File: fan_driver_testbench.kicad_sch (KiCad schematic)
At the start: 6 parts, among them Q5 BTS141

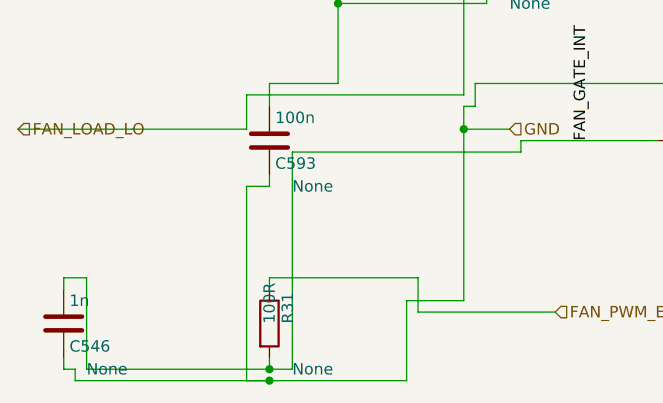
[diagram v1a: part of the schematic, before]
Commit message: optimazed load to kicad
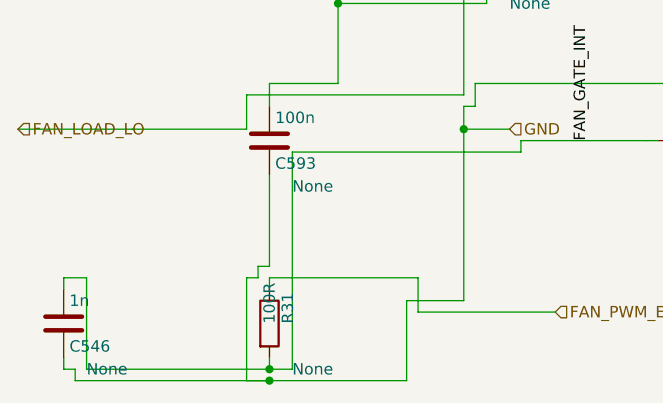
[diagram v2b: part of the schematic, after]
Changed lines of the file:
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@@
 		(instances
 			(project "Untitled"
-				(path "/4b1f6fb3-968a-4690-9ff6-6727556273b3"
+				(path "/bf864d83-638d-4400-a181-9f7b7e09d144"
 					(reference "R31")
 					(unit 1)
@@
 		(instances
 			(project "Untitled"
-				(path "/4b1f6fb3-968a-4690-9ff6-6727556273b3"
+				(path "/bf864d83-638d-4400-a181-9f7b7e09d144"
 					(reference "C546")
 					(unit 1)
@@
 		(instances
 			(project "Untitled"
-				(path "/4b1f6fb3-968a-4690-9ff6-6727556273b3"
+				(path "/bf864d83-638d-4400-a181-9f7b7e09d144"
 					(reference "Q5")
 					(unit 1)
@@
 		(instances
 			(project "Untitled"
-				(path "/4b1f6fb3-968a-4690-9ff6-6727556273b3"
+				(path "/bf864d83-638d-4400-a181-9f7b7e09d144"
 					(reference "D6")
 					(unit 1)
@@
 		(instances
 			(project "Untitled"
-				(path "/4b1f6fb3-968a-4690-9ff6-6727556273b3"
+				(path "/bf864d83-638d-4400-a181-9f7b7e09d144"
 					(reference "L637")
 					(unit 1)
@@
 		(instances
 			(project "Untitled"
-				(path "/4b1f6fb3-968a-4690-9ff6-6727556273b3"
+				(path "/bf864d83-638d-4400-a181-9f7b7e09d144"
 					(reference "C593")
 					(unit 1)
@@
 	(wire
 		(pts
-			(xy 31.75 33.02) (xy 29.21 33.02)
-		)
-		(stroke
-			(width 0)
-			(type default)
-		)
-	)
-	(wire
-		(pts
-			(xy 29.21 33.02) (xy 29.21 54.61)
-		)
-		(stroke
+			(xy 31.75 33.02) (xy 31.75 41.91)
+		)
+		(stroke
+			(width 0)
+			(type default)
+		)
+	)
+	(wire
+		(pts
+			(xy 31.75 41.91) (xy 30.48 41.91)
+		)
+		(stroke
+			(width 0)
+			(type default)
+		)
+	)
+	(wire
+		(pts
+			(xy 30.48 41.91) (xy 30.48 43.18)
+		)
+		(stroke
+			(width 0)
+			(type default)
+		)
+	)
+	(wire
+		(pts
+			(xy 30.48 43.18) (xy 29.21 43.18)
+		)
+		(stroke
+			(width 0)
+			(type default)
+		)
+	)
+	(wire
+		(pts
+			(xy 29.21 43.18) (xy 29.21 54.61)
+		)
+		(stroke

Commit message: tests_fix
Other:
- title: (none) -> climate_control_niva_travel
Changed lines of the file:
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@@
 	(generator_version "9.0")
 	(paper "A4")
+	(title_block
+		(title "climate_control_niva_travel")
+	)
 	(symbol
 		(lib_id "Device:R")
@@
 		)
 		(instances
-			(project "Untitled"
-				(path "/bf864d83-638d-4400-a181-9f7b7e09d144"
+			(project "climate_control_niva_travel"
+				(path "/769b9906-d389-4980-b175-619cd77c101f"
 					(reference "R31")
 					(unit 1)
@@
 		)
 		(instances
-			(project "Untitled"
-				(path "/bf864d83-638d-4400-a181-9f7b7e09d144"
+			(project "climate_control_niva_travel"
+				(path "/769b9906-d389-4980-b175-619cd77c101f"
 					(reference "C546")
 					(unit 1)
@@
 		)
 		(instances
-			(project "Untitled"
-				(path "/bf864d83-638d-4400-a181-9f7b7e09d144"
+			(project "climate_control_niva_travel"
+				(path "/769b9906-d389-4980-b175-619cd77c101f"
 					(reference "Q5")
 					(unit 1)
@@
 		)
 		(instances
-			(project "Untitled"
-				(path "/bf864d83-638d-4400-a181-9f7b7e09d144"
+			(project "climate_control_niva_travel"
+				(path "/769b9906-d389-4980-b175-619cd77c101f"
 					(reference "D6")
 					(unit 1)
@@
 		)
 		(instances
-			(project "Untitled"
-				(path "/bf864d83-638d-4400-a181-9f7b7e09d144"
+			(project "climate_control_niva_travel"
+				(path "/769b9906-d389-4980-b175-619cd77c101f"
 					(reference "L637")
 					(unit 1)
@@
 		)
 		(instances
-			(project "Untitled"
-				(path "/bf864d83-638d-4400-a181-9f7b7e09d144"
+			(project "climate_control_niva_travel"
+				(path "/769b9906-d389-4980-b175-619cd77c101f"
 					(reference "C593")
 					(unit 1)
@@
 	(junction
 		(at 31.75 54.61)
+		(diameter 0)
+		(color 0 0 0 0)
+	)
+	(junction
+		(at 67.31 27.94)
 		(diameter 0)
 		(color 0 0 0 0)
@@
 		)
 	)
+	(hierarchical_label "FAN_LOAD_LO"
+		(shape output)
+		(at 3.81 26.67 0)
+		(effects
+			(font
+				(size 1.27 1.27)
+			)
+			(justify left)
+		)
+	)
+	(hierarchical_label "MOTOR_TERM"
+		(shape output)
+		(at 26.67 6.35 0)
+		(effects
+			(font
+				(size 1.27 1.27)
+			)
+			(justify left)
+		)
+	)
 	(hierarchical_label "VBAT_FAN"
 		(shape input)
@@
 		(effects
 			(font
-				(size 1.27 1.27)
-			)
-			(justify left)
-		)
-	)
-	(hierarchical_label "FAN_LOAD_LO"
-		(shape input)
-		(at 3.81 26.67 0)
-		(effects
-			(font
-				(size 1.27 1.27)
-			)
-			(justify left)
-		)
-	)
-	(hierarchical_label "MOTOR_TERM"
-		(shape input)
-		(at 26.67 6.35 0)
-		(effects
-			(font

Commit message: refactoring
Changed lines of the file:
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@@
+			)
+		)
+		(property "Sim.Device" "R"
+			(at 34.29 53.3399 0)
+			(effects
+				(font
+					(size 1.27 1.27)
+				)
+				(justify left)
+			)
+		)
+		(property "Sim.Params" "R=100R"
+			(at 34.29 53.3399 0)
+			(effects
+				(font
+					(size 1.27 1.27)
+				)
+				(justify left)
 			)
 		)
@@
 		(instances
 			(project "climate_control_niva_travel"
-				(path "/769b9906-d389-4980-b175-619cd77c101f"
+				(path "/04e9baa8-05c1-4d46-8e7f-66f0ccb7f2e0"
 					(reference "R31")
 					(unit 1)
@@
 			)
 		)
+		(property "Sim.Device" "C"
+			(at 11.43 53.3399 0)
+			(effects
+				(font
+					(size 1.27 1.27)
+				)
+				(justify left)
+			)
+		)
+		(property "Sim.Params" "C=1n"
+			(at 11.43 53.3399 0)
+			(effects
+				(font
+					(size 1.27 1.27)
+				)
+				(justify left)
+			)
+		)
 		(pin "1"
 		)
@@
 		(instances
 			(project "climate_control_niva_travel"
-				(path "/769b9906-d389-4980-b175-619cd77c101f"
+				(path "/04e9baa8-05c1-4d46-8e7f-66f0ccb7f2e0"
 					(reference "C546")
 					(unit 1)
@@
 			)
 		)
+		(property "Sim.Device" "X"
+			(at 82.55 33.0199 0)
+			(effects
+				(font
+					(size 1.27 1.27)
+				)
+				(justify left)
+			)
+		)
+		(property "Sim.Name" "BTS141"
+			(at 82.55 33.0199 0)
+			(effects
+				(font
+					(size 1.27 1.27)
+				)
+				(justify left)
+			)
+		)
+		(property "Sim.Library" "${KIPRJMOD}/spice/lib/BTS141_model.lib"
+			(at 82.55 33.0199 0)
+			(effects
+				(font
+					(size 1.27 1.27)
+				)
+				(justify left)
+			)
+		)
+		(property "Sim.Pins" "1=IN 2=OUT 3=GND"
+			(at 82.55 33.0199 0)
+			(effects
+				(font
+					(size 1.27 1.27)
+				)
+				(justify left)
+			)
+		)
+		(property "Sim.Enable" "1"
+			(at 82.55 33.0199 0)
+			(effects
+				(font
+					(size 1.27 1.27)
+				)
+				(justify left)
+			)
+		)
 		(pin "1"
 		)
@@
 		(instances
 			(project "climate_control_niva_travel"
-				(path "/769b9906-d389-4980-b175-619cd77c101f"
+				(path "/04e9baa8-05c1-4d46-8e7f-66f0ccb7f2e0"
 					(reference "Q5")
 					(unit 1)
@@
 			)
 		)
+		(property "Sim.Device" "D"
+			(at 81.28 12.6999 0)
+			(effects
+				(font
+					(size 1.27 1.27)
+				)
+				(justify left)
+			)
+		)
+		(property "Sim.Model" "D_SCHOTTKY"
+			(at 81.28 12.6999 0)
+			(effects
+				(font
+					(size 1.27 1.27)
+				)
+				(justify left)
+			)
+		)
+		(property "Sim.Params" "D(IS=1e-6 RS=0.03 N=1.05 CJO=200p VJ=0.55 M=0.5 BV=40 IBV=1e-4)"
+			(at 81.28 12.6999 0)
+			(effects
+				(font
+					(size 1.27 1.27)
+				)
+				(justify left)
+			)
+		)
 		(pin "1"
 		)
@@
 		(instances
 			(project "climate_control_niva_travel"
-				(path "/769b9906-d389-4980-b175-619cd77c101f"
+				(path "/04e9baa8-05c1-4d46-8e7f-66f0ccb7f2e0"
 					(reference "D6")
 					(unit 1)
@@
 			)
 		)
+		(property "Sim.Device" "L"
+			(at 58.42 12.6999 0)
+			(effects
+				(font
+					(size 1.27 1.27)
+				)
+				(justify left)
+			)
+		)
+		(property "Sim.Params" "L=2u"
+			(at 58.42 12.6999 0)
+			(effects
+				(font
+					(size 1.27 1.27)
+				)
+				(justify left)
+			)
+		)
 		(pin "1"
 		)
@@
 		(instances
 			(project "climate_control_niva_travel"
-				(path "/769b9906-d389-4980-b175-619cd77c101f"
+				(path "/04e9baa8-05c1-4d46-8e7f-66f0ccb7f2e0"
 					(reference "L637")
 					(unit 1)
@@
 			)
 		)
+		(property "Sim.Device" "C"
+			(at 34.29 33.0199 0)
+			(effects
+				(font
+					(size 1.27 1.27)
+				)
+				(justify left)
+			)
+		)
+		(property "Sim.Params" "C=100n"
+			(at 34.29 33.0199 0)
+			(effects
+				(font
+					(size 1.27 1.27)
+				)
+				(justify left)
+			)
+		)
 		(pin "1"
 		)
@@
 		(instances
 			(project "climate_control_niva_travel"
-				(path "/769b9906-d389-4980-b175-619cd77c101f"
+				(path "/04e9baa8-05c1-4d46-8e7f-66f0ccb7f2e0"
 					(reference "C593")
 					(unit 1)
@@
 	(junction
 		(at 31.75 53.34)
-		(diameter 0)
+		(diameter 0.0000)
 		(color 0 0 0 0)
 	)
 	(junction
 		(at 83.82 7.62)
-		(diameter 0)
+		(diameter 0.0000)
 		(color 0 0 0 0)
 	)
 	(junction
 		(at 55.88 2.54)
-		(diameter 0)
+		(diameter 0.0000)
 		(color 0 0 0 0)
 	)
 	(junction
 		(at 39.37 12.7)
-		(diameter 0)
+		(diameter 0.0000)
 		(color 0 0 0 0)
 	)
 	(junction
 		(at 53.34 26.67)
-		(diameter 0)
+		(diameter 0.0000)
 		(color 0 0 0 0)
 	)
 	(junction
 		(at 31.75 54.61)
-		(diameter 0)
+		(diameter 0.0000)
 		(color 0 0 0 0)
 	)
 	(junction
 		(at 67.31 27.94)
-		(diameter 0)
+		(diameter 0.0000)
 		(color 0 0 0 0)
 	)

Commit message: fix
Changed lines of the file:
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@@
 				(instances
 			(project "climate_control_niva_travel"
-				(path "/9d65f2b6-eafc-4877-87dc-8b71e3390a39"(reference "R31") (unit 1) )
+				(path "/3bdb15f9-9517-4ddf-9f93-5c92d7358861"(reference "R31") (unit 1) )
 			)
 		)
@@
 				(instances
 			(project "climate_control_niva_travel"
-				(path "/9d65f2b6-eafc-4877-87dc-8b71e3390a39"(reference "C546") (unit 1) )
+				(path "/3bdb15f9-9517-4ddf-9f93-5c92d7358861"(reference "C546") (unit 1) )
 			)
 		)
@@
 				(instances
 			(project "climate_control_niva_travel"
-				(path "/9d65f2b6-eafc-4877-87dc-8b71e3390a39"(reference "Q5") (unit 1) )
+				(path "/3bdb15f9-9517-4ddf-9f93-5c92d7358861"(reference "Q5") (unit 1) )
 			)
 		)
@@
 				(instances
 			(project "climate_control_niva_travel"
-				(path "/9d65f2b6-eafc-4877-87dc-8b71e3390a39"(reference "D6") (unit 1) )
+				(path "/3bdb15f9-9517-4ddf-9f93-5c92d7358861"(reference "D6") (unit 1) )
 			)
 		)
@@
 				(instances
 			(project "climate_control_niva_travel"
-				(path "/9d65f2b6-eafc-4877-87dc-8b71e3390a39"(reference "L637") (unit 1) )
+				(path "/3bdb15f9-9517-4ddf-9f93-5c92d7358861"(reference "L637") (unit 1) )
 			)
 		)
@@
 				(instances
 			(project "climate_control_niva_travel"
-				(path "/9d65f2b6-eafc-4877-87dc-8b71e3390a39"(reference "C593") (unit 1) )
+				(path "/3bdb15f9-9517-4ddf-9f93-5c92d7358861"(reference "C593") (unit 1) )
 			)
 		)
@@
 		(pts
 			(xy 29.21 43.18) (xy 29.21 54.61)
-		)
-		(stroke
-			(width 0)
-			(type default)
-		)
-	)
-	(wire
-		(pts
-			(xy 29.21 54.61) (xy 31.75 54.61)
 		)
 		(stroke
@@
 	)
 	(junction
-		(at 31.75 54.61)
+		(at 29.21 54.61)
 		(diameter 0.0000)
 		(color 0 0 0 0)
